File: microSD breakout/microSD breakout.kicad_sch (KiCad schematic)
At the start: 4 parts, among them J1 Micro_SD_Card_Det_1Pin, J2 Conn_01x07

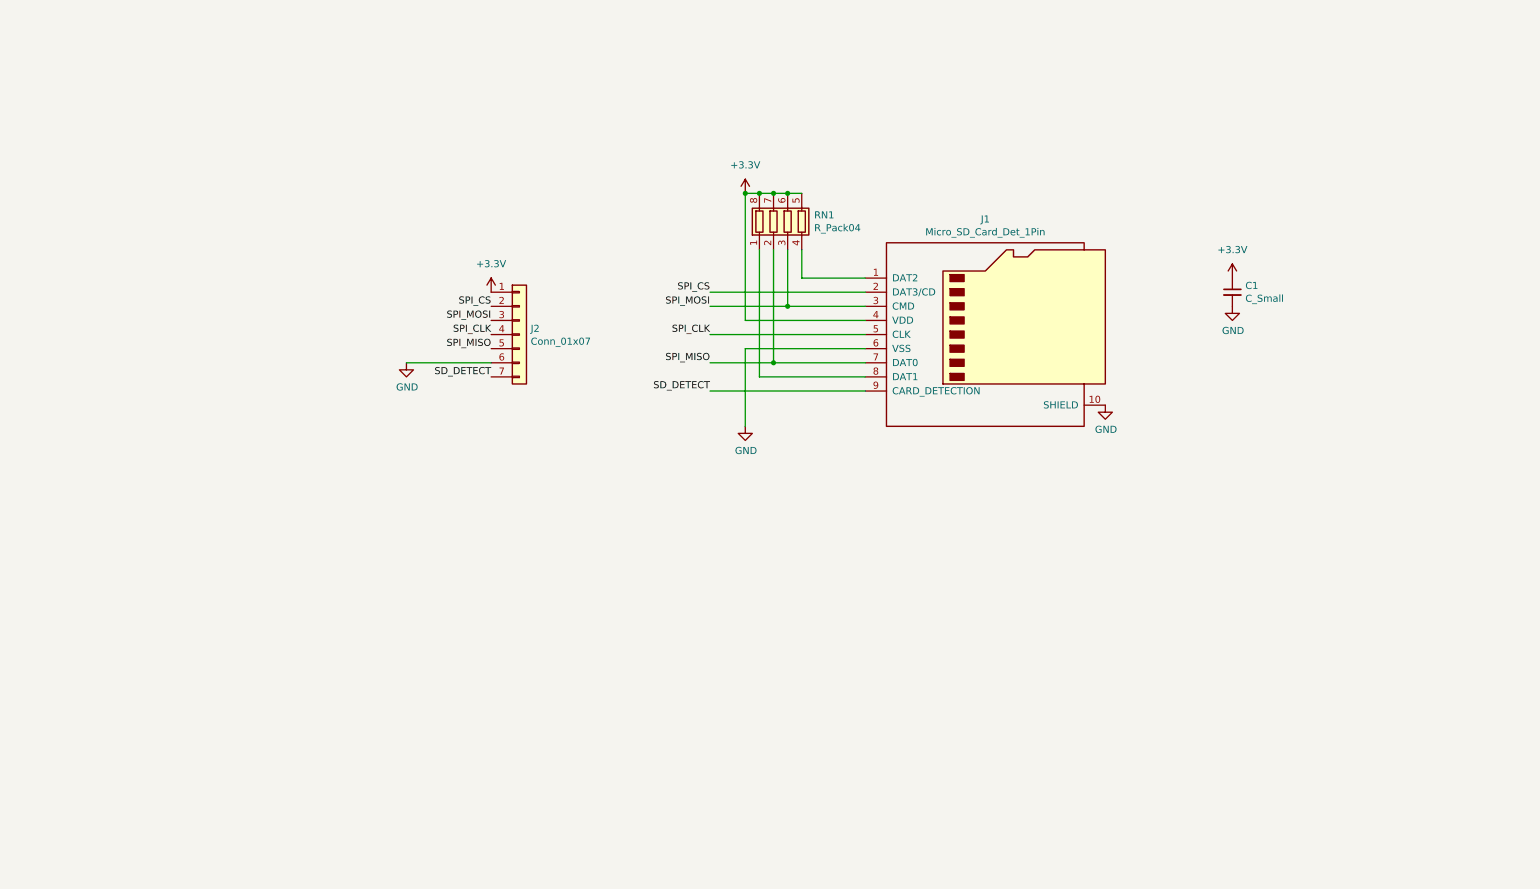
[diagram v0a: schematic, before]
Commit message: Addition of 'microSD breakout' which is in fact an extension cable adapter that may work with my PiStorm'X boards. Renamed the microSD SPI socket breakout as 'microSD socket breakout'.
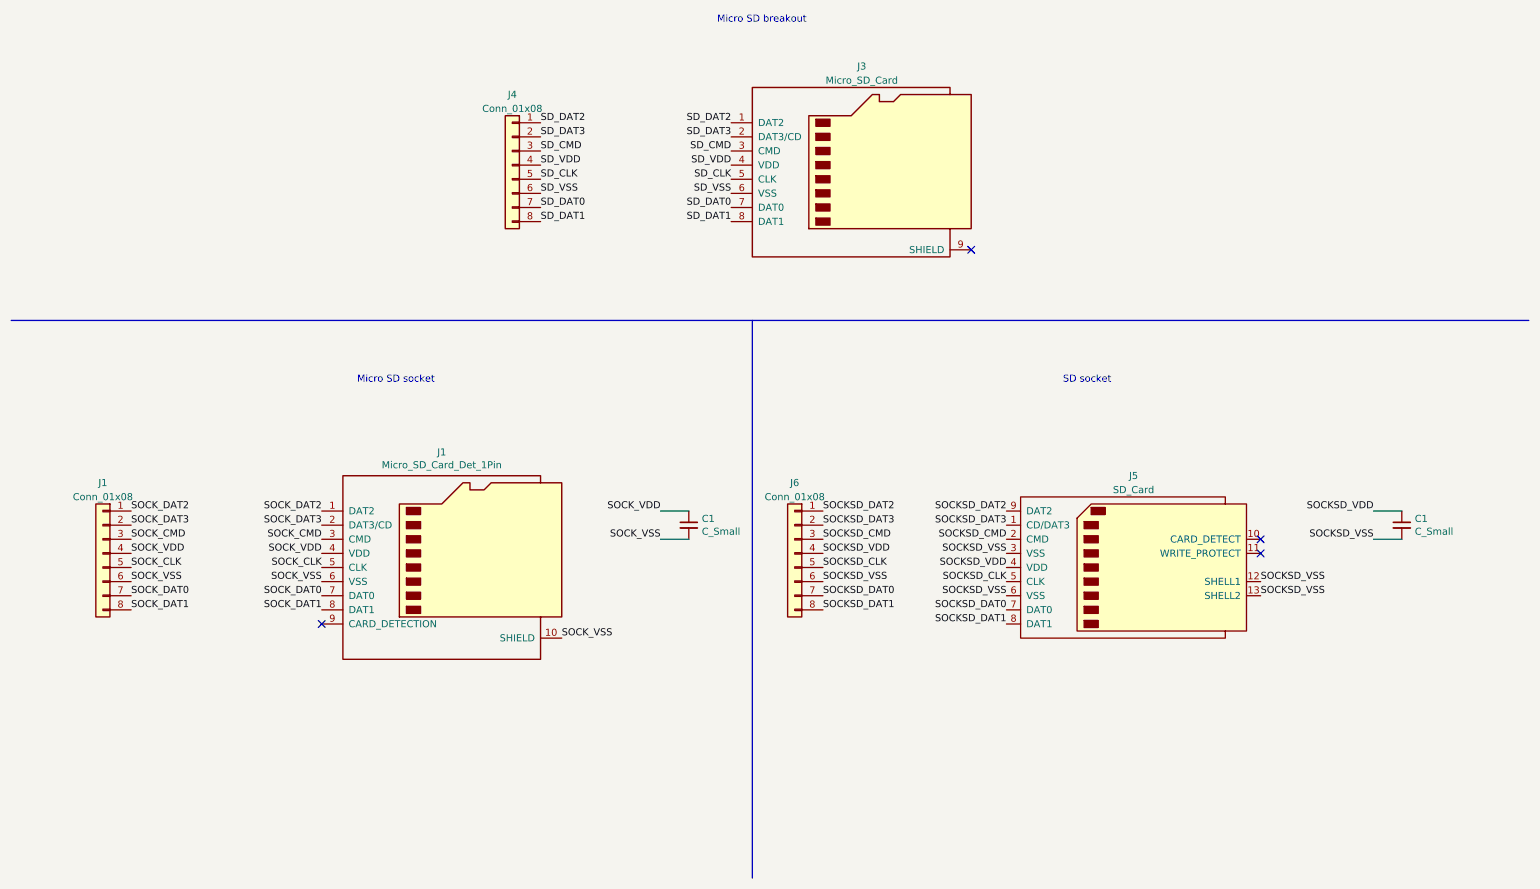
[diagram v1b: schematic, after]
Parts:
- removed C1: C_Small, Capacitor_SMD:C_0805_2012Metric, symbol Device:C_Small
- removed J2: Conn_01x07, Connector_PinHeader_2.54mm:PinHeader_1x07_P2.54mm_Vertical, symbol Connector_Generic:Conn_01x07
- removed RN1: R_Pack04, Resistor_SMD:R_Array_Convex_4x0603, symbol Device:R_Pack04
- added C1 (x2): C_Small, Capacitor_SMD:C_0805_2012Metric, symbol Device:C_Small
- added J1, J4, J6: Conn_01x08, Connector_PinHeader_1.27mm:PinHeader_1x08_P1.27mm_Vertical, symbol Connector_Generic:Conn_01x08
- added J3: Micro_SD_Card, Sassa:Micro_SD, symbol Connector:Micro_SD_Card
- added J5: SD_Card, Sassa:Conn_SDcard, symbol Connector:SD_Card
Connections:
- net SOCK_DAT2: now reaches J1.1 (DAT2)
- net SOCK_DAT2: now also J1.1 (Pin_1)
- net SOCK_DAT1: now reaches J1.8 (DAT1)
- net SOCK_DAT1: now also J1.8 (Pin_8)
- net +3.3V renamed SOCK_VDD
- net SOCK_VDD: now also C1.1, J1.4 (Pin_4)
- net GND renamed SOCK_VSS
- net SOCK_VSS: now also C1.2, J1.6 (Pin_6)
- net SD_DETECT: no longer names the net of J1.9 (CARD_DETECTION)
- net SPI_CLK renamed SOCK_CLK
- net SOCK_CLK: now also J1.5 (Pin_5)
- net SPI_CS renamed SOCK_DAT3
- net SOCK_DAT3: now also J1.2 (Pin_2)
- net SPI_MISO renamed SOCK_DAT0
- net SOCK_DAT0: now also J1.7 (Pin_7)
- net SPI_MOSI renamed SOCK_CMD
- net SOCK_CMD: now also J1.3 (Pin_3)
- new net SD_CLK: J3.5 (CLK), J4.5 (Pin_5)
- new net SD_CMD: J3.3 (CMD), J4.3 (Pin_3)
- new net SD_DAT0: J3.7 (DAT0), J4.7 (Pin_7)
- new net SD_DAT1: J3.8 (DAT1), J4.8 (Pin_8)
- new net SD_DAT2: J3.1 (DAT2), J4.1 (Pin_1)
- new net SD_DAT3: J3.2 (DAT3/CD), J4.2 (Pin_2)
- new net SD_VDD: J3.4 (VDD), J4.4 (Pin_4)
- new net SD_VSS: J3.6 (VSS), J4.6 (Pin_6)
- new net SOCKSD_CLK: J5.5 (CLK), J6.5 (Pin_5)
- new net SOCKSD_CMD: J5.2 (CMD), J6.3 (Pin_3)
- new net SOCKSD_DAT0: J5.7 (DAT0), J6.7 (Pin_7)
- new net SOCKSD_DAT1: J5.8 (DAT1), J6.8 (Pin_8)
- new net SOCKSD_DAT2: J5.9 (DAT2), J6.1 (Pin_1)
- new net SOCKSD_DAT3: J5.1 (CD/DAT3), J6.2 (Pin_2)
- new net SOCKSD_VDD: C1.1, J5.4 (VDD), J6.4 (Pin_4)
- new net SOCKSD_VSS: C1.2, J5.12 (SHELL1), J5.13 (SHELL2), J5.3 (VSS), J5.6 (VSS), J6.6 (Pin_6)
- no-connect marks 0 -> 4
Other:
- note added: "Micro SD breakout"
- note added: "Micro SD socket"
- note added: "SD socket"
- company: (none) -> FLACO
- title: (none) -> microSD breakout
